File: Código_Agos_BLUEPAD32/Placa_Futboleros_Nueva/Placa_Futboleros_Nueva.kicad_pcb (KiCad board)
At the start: 2 copper layers, 72 x 72 mm, 16 parts, among them J1 BAT, J2 Motor1, J3 Motor2, U1 AMS1117, U3 DRV8833, U4 DRV8833, U5 esp32_36_pins-custom_library

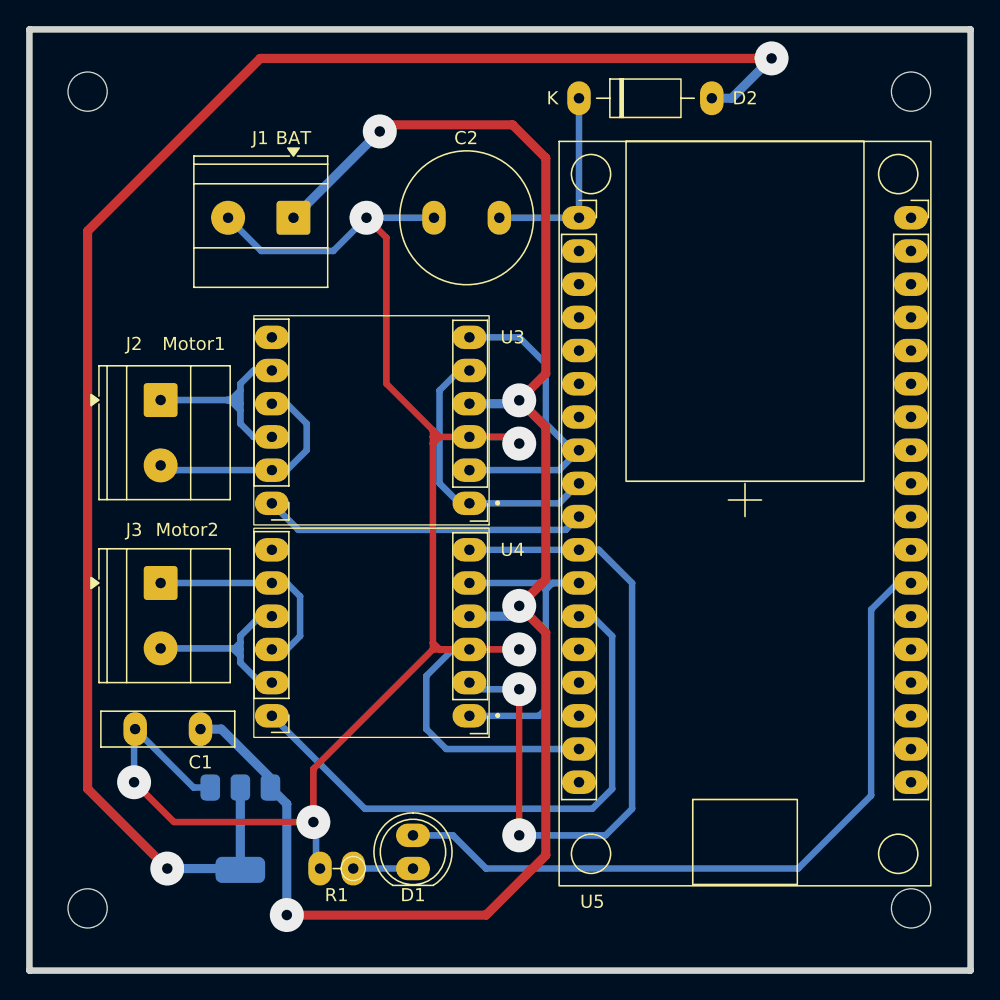
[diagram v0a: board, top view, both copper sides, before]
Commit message: Mejoras en la Nueva Placa Futboleros
Se colocan conectores molex jst en lugar de borneras para conectar motores y batería.
Se cambia el capacitor electrolítico de 470uF.
Se crea la placa para soldar a los motores y con conectores
jst conectar la placa a los molex de la placa maestra
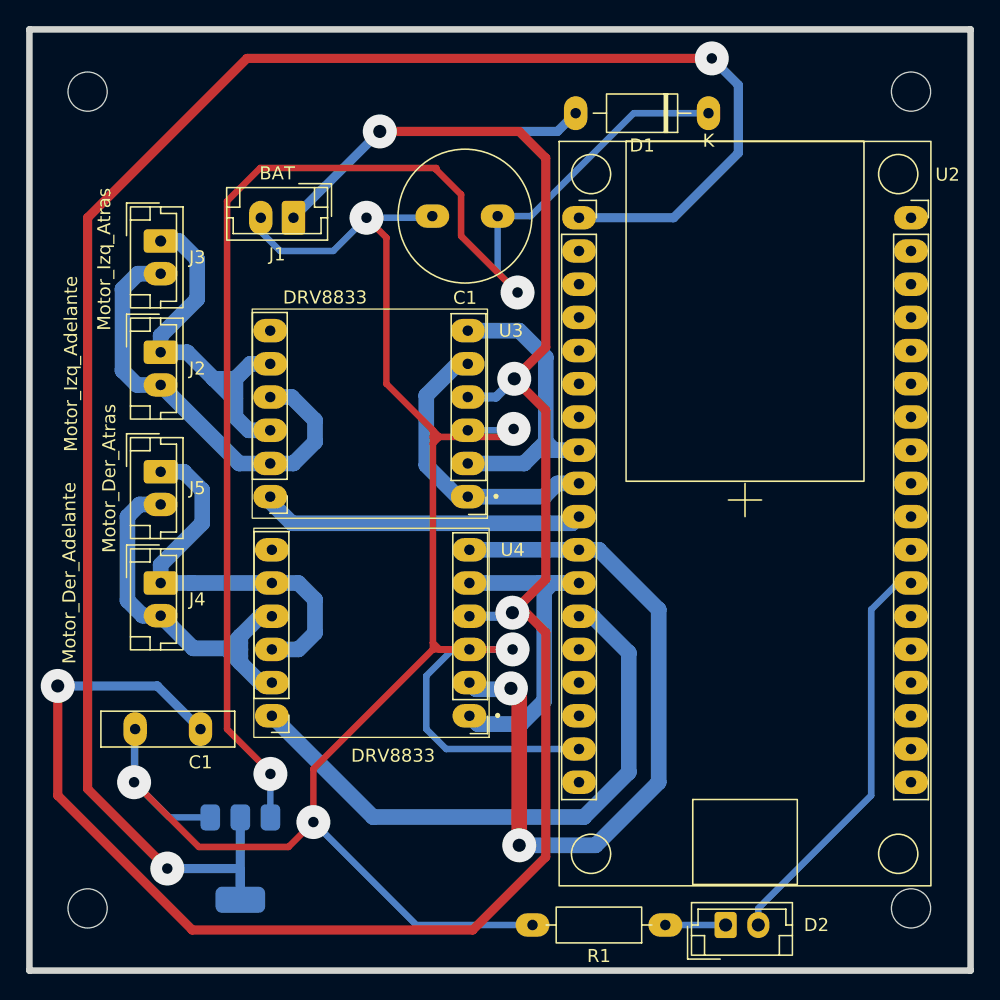
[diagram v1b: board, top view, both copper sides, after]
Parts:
- removed C2: 470uF, Capacitor_THT:C_Radial_D10.0mm_H12.5mm_P5.00mm
- removed the D2 at (108.2, 37.6)
- added C1: 470uF, Capacitor_THT:C_Radial_D10.0mm_H12.5mm_P5.00mm, F.Cu at (102.0, 46.6)
- added D1: 1N5819, Diode_THT:D_DO-41_SOD81_P10.16mm_Horizontal, F.Cu at (118.1, 38.7)
- added J3: Motor_Izq_Atras, Connector_JST:JST_EH_B2B-EH-A_1x02_P2.50mm_Vertical, F.Cu at (76.2, 48.5)
- added J5: Motor_Der_Atras, Connector_JST:JST_EH_B2B-EH-A_1x02_P2.50mm_Vertical, F.Cu at (76.2, 66.2)
- D2: renamed from D1; footprint LED_THT:LED_D5.0mm -> Connector_JST:JST_EH_B2B-EH-A_1x02_P2.50mm_Vertical
- J1: footprint TerminalBlock_Phoenix:TerminalBlock_Phoenix_MKDS-1,5-2_1x02_P5.00mm_Horizontal -> Connector_JST:JST_EH_B2B-EH-A_1x02_P2.50mm_Vertical
- J2: value Motor1 -> Motor_Izq_Adelante; footprint TerminalBlock_Phoenix:TerminalBlock_Phoenix_MKDS-1,5-2_1x02_P5.00mm_Horizontal -> Connector_JST:JST_EH_B2B-EH-A_1x02_P2.50mm_Vertical
- J4: renamed from J3; value Motor2 -> Motor_Der_Adelante; footprint TerminalBlock_Phoenix:TerminalBlock_Phoenix_MKDS-1,5-2_1x02_P5.00mm_Horizontal -> Connector_JST:JST_EH_B2B-EH-A_1x02_P2.50mm_Vertical
- R1: footprint Resistor_THT:R_Axial_DIN0204_L3.6mm_D1.6mm_P2.54mm_Vertical -> Resistor_THT:R_Axial_DIN0207_L6.3mm_D2.5mm_P10.16mm_Horizontal
- moved D2 24.3 mm to (119.4, 100.8), turned to 0 degrees
- moved R1 24.3 mm to (114.8, 100.8)
- moved J2 3.66 mm to (76.2, 57.0)
- moved U1 2.29 mm to (82.3, 95.8)
- moved U3 0.52 mm to (91.8, 51.8)
- renumbered U5 to U2
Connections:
- U1 pad 3: VCC -> Net-(D1-K)
- U2 pad 1: Net-(D2-K) (its old number) -> +5V
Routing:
- net Net-(D1-K): track 0.00 -> 103.5 mm, vias 0 -> 2
- net VCC: track 127.7 -> 169.1 mm
- net LED_Encendido: track 56.5 -> 31.6 mm
- net GND: track 145.4 -> 163.8 mm
- net Net-(J2-Pin_2): track 17.3 -> 33.8 mm
- net Net-(J4-Pin_2): track 15.7 -> 32.1 mm
- net Net-(D2-K) (its old number): track 15.2 -> 0.00 mm
- net +5V: track 126.9 -> 141.7 mm
- net Net-(J4-Pin_1): track 16.7 -> 31.0 mm
- net Net-(J2-Pin_1): track 17.6 -> 29.6 mm
- net IN_M2B: track 55.4 -> 57.9 mm
- net SLEEP_M2: track 44.5 -> 46.0 mm
- net IN_M1A: track 22.0 -> 22.6 mm
